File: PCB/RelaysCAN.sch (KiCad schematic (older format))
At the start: 24 parts, among them J1 Screw_Terminal_01x03, J2 Screw_Terminal_01x02, J3 Conn_01x24_Male, J4 Conn_01x24_Male, J5 Conn_01x24_Male, J6 Conn_01x24_Male, J7 Conn_01x24_Male, J8 Conn_01x24_Male, U1 MCP2562-E-P, U2 MCP2515-IP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

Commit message: Update PCB.
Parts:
- added C6, C7: 22pF, Capacitor_THT:C_Disc_D4.3mm_W1.9mm_P5.00mm, symbol Device:C
- added JP2: SolderJumper_2_Bridged, Jumper:SolderJumper-2_P1.3mm_Open_RoundedPad1.0x1.5mm, symbol Jumper:SolderJumper_2_Bridged
- added Y1: 16MHz, Crystal:Crystal_HC18-U_Vertical, symbol Device:Crystal
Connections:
- net CLKO: now also JP2.2 (B); no longer U2.8 (OSC1)
- net GND: now also C6.2, C7.2
- net CLKOUT: now reaches U3.9 (XTAL1/PB6)
- net CLKOUT: now also U2.3 (CLKOUT/SOF)
- net at U2.7 (OSC2): now also C7.1, Y1.2
- new net: C6.1, JP2.1 (A), U2.8 (OSC1), Y1.1
- no-connect marks 15 -> 12
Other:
- moved on the sheet: C2, C3, U2

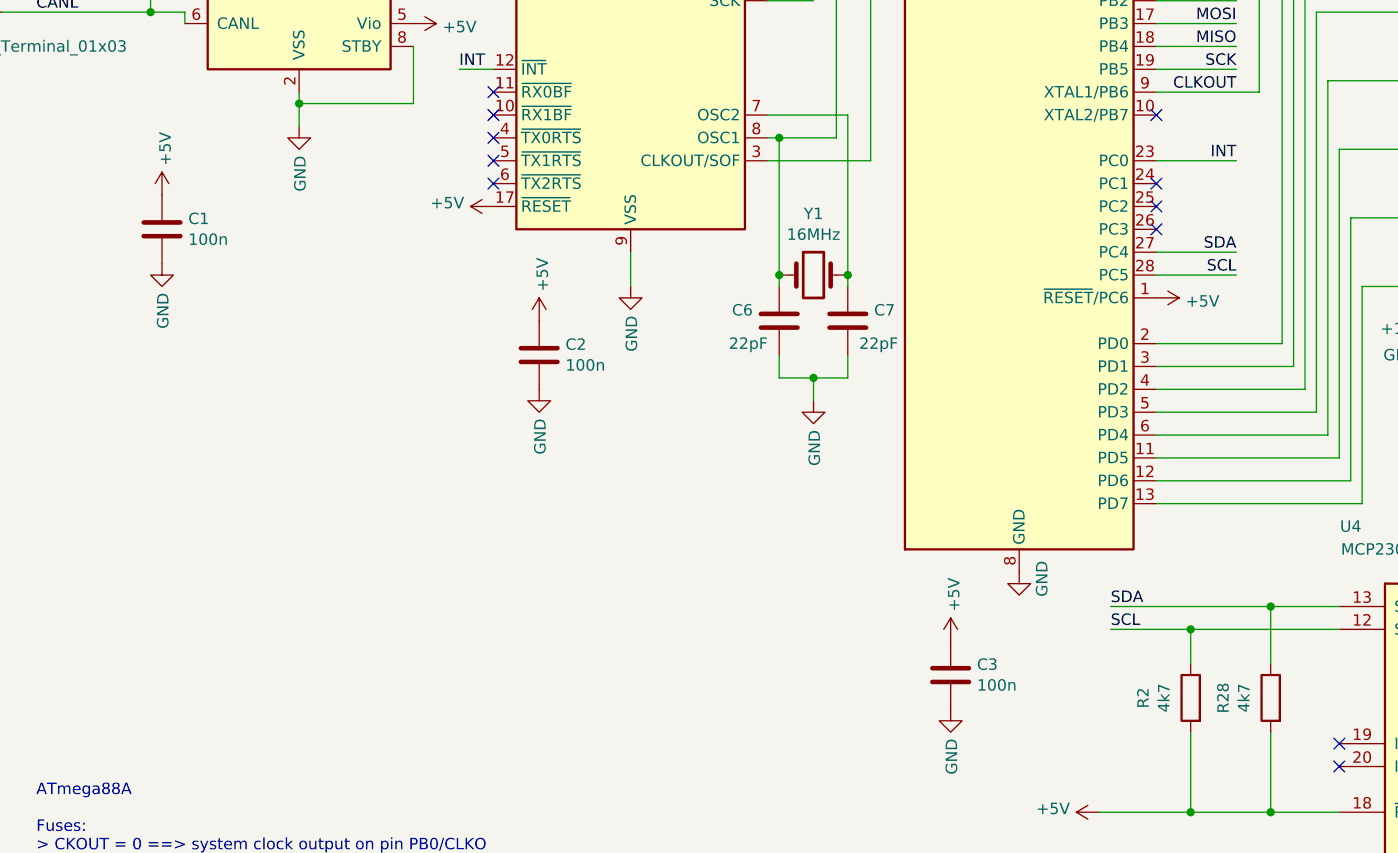
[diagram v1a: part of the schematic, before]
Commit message: Add a jumper to enter configuration mode.
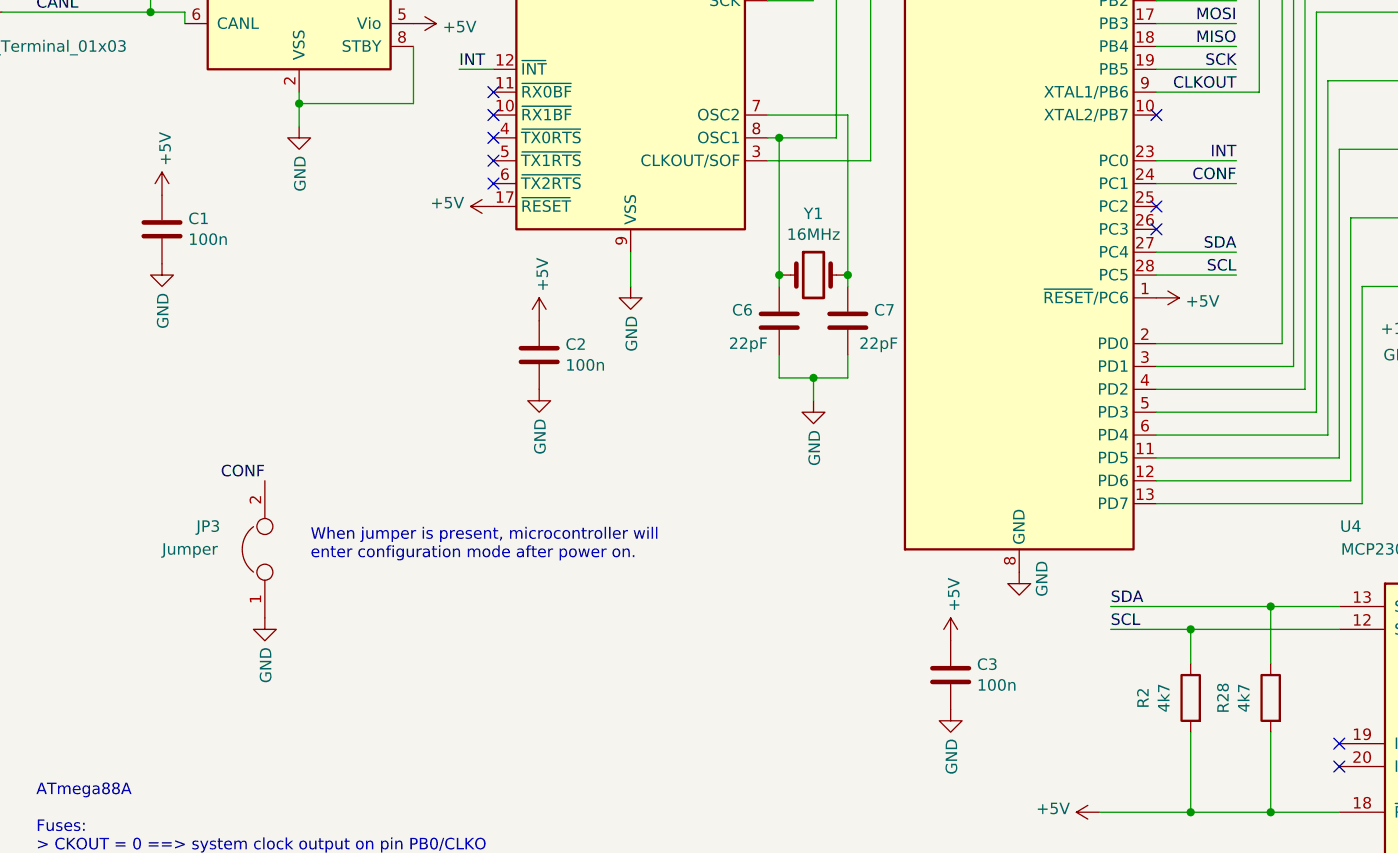
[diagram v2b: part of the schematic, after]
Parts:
- added JP3: Jumper, Connector_PinHeader_2.54mm:PinHeader_1x02_P2.54mm_Vertical, symbol Device:Jumper
- JP1: footprint Connector_PinHeader_2.54mm:PinHeader_1x02_P2.54mm_Horizontal -> Connector_PinHeader_2.54mm:PinHeader_1x02_P2.54mm_Vertical
- R1: footprint Resistor_THT:R_Axial_DIN0207_L6.3mm_D2.5mm_P10.16mm_Horizontal -> Resistor_THT:R_Axial_DIN0207_L6.3mm_D2.5mm_P5.08mm_Vertical
- U3, U4: footprint Package_DIP:DIP-28_W7.62mm -> Package_DIP:DIP-28_W7.62mm_LongPads
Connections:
- net GND: now also JP3.1
- net CONF: now reaches U3.24 (PC1)
- net CONF: now also JP3.2
- no-connect marks 12 -> 11
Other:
- note added: "When jumper is present, microcontroller will\nenter configuration mode after power on."
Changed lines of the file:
@@
 F 0 "U3" H 5500 4150 50  0000 R CNN
 F 1 "ATmega88A-PU" H 6000 4050 50  0000 R CNN
-F 2 "Package_DIP:DIP-28_W7.62mm" H 5250 2550 50  0001 C CIN
+F 2 "Package_DIP:DIP-28_W7.62mm_LongPads" H 5250 2550 50  0001 C CIN
 F 3 "http://ww1.microchip.com/downloads/en/DeviceDoc/ATmega48A_88A_168A-Data-Sheet-40002007A.pdf" H 5250 2550 50  0001 C CNN
 	1    5250 2550
@@
 F 0 "U4" H 6700 6150 50  0000 C CNN
 F 1 "MCP23017_SP" H 6900 6050 50  0000 C CNN
-F 2 "Package_DIP:DIP-28_W7.62mm" H 7550 4000 50  0001 L CNN
+F 2 "Package_DIP:DIP-28_W7.62mm_LongPads" H 7550 4000 50  0001 L CNN
 F 3 "http://ww1.microchip.com/downloads/en/DeviceDoc/20001952C.pdf" H 7550 3900 50  0001 L CNN
 	1    7350 5000
@@
 F 0 "R1" V 1250 1000 50  0000 C CNN
 F 1 "120R" V 1350 1000 50  0000 C CNN
-F 2 "Resistor_THT:R_Axial_DIN0207_L6.3mm_D2.5mm_P10.16mm_Horizontal" V 1380 1000 50  0001 C CNN
+F 2 "Resistor_THT:R_Axial_DIN0207_L6.3mm_D2.5mm_P5.08mm_Vertical" V 1380 1000 50  0001 C CNN
 F 3 "~" H 1450 1000 50  0001 C CNN
 	1    1450 1000
@@
 F 0 "JP1" V 1400 1300 50  0000 R CNN
 F 1 "Jumper" V 1300 1450 50  0000 R CNN
-F 2 "Connector_PinHeader_2.54mm:PinHeader_1x02_P2.54mm_Horizontal" H 1300 1000 50  0001 C CNN
+F 2 "Connector_PinHeader_2.54mm:PinHeader_1x02_P2.54mm_Vertical" H 1300 1000 50  0001 C CNN
 F 3 "~" H 1300 1000 50  0001 C CNN
 	1    1300 1000
@@
 NoConn ~ 5850 1450
 NoConn ~ 5850 2050
-NoConn ~ 5850 2350
 NoConn ~ 5850 2450
 NoConn ~ 5850 2550
@@
 Wire Wire Line
 	6400 3050 6400 700
-Wire Wire Line
-	6400 700  7250 700
-Wire Wire Line
-	6450 1000 7250 1000
-Wire Wire Line
-	6500 1300 7250 1300
 Wire Wire Line
 	6550 1600 7250 1600
@@
 Wire Wire Line
 	4450 650  4450 2150
+Wire Wire Line
+	6500 1300 7250 1300
+Wire Wire Line
+	6450 1000 7250 1000
+Wire Wire Line
+	6400 700  7250 700
+Text Label 6200 2350 2    50   ~ 0
+CONF
+Wire Wire Line
+	5850 2350 6200 2350
+$Comp
+L Device:Jumper JP3
+U 1 1 610688EB
+P 1950 3950
+F 0 "JP3" V 2050 4250 50  0000 R CNN
+F 1 "Jumper" V 1950 4400 50  0000 R CNN
+F 2 "Connector_PinHeader_2.54mm:PinHeader_1x02_P2.54mm_Vertical" H 1950 3950 50  0001 C CNN
+F 3 "~" H 1950 3950 50  0001 C CNN
+	1    1950 3950
+	0    -1   -1   0
+$EndComp
+$Comp
+L power:GND #PWR034
+U 1 1 61069EA3
+P 1950 4250
+F 0 "#PWR034" H 1950 4000 50  0001 C CNN
+F 1 "GND" V 1955 4122 50  0000 R CNN
+F 2 "" H 1950 4250 50  0001 C CNN
+F 3 "" H 1950 4250 50  0001 C CNN
+	1    1950 4250
+	1    0    0    -1
+$EndComp
+Text Label 1950 3650 2    50   ~ 0
+CONF
+Text Notes 2150 4000 0    50   ~ 0
+When jumper is present, microcontroller will\nenter configuration mode after power on.
 $EndSCHEMATC
